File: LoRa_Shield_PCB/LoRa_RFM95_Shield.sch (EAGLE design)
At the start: 0 parts

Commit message: LoRa shield PCB power circuits
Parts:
- added B1: ARDUINO_SHIELD, SparkFun-Boards:ARDUINO_UNO_R3_SHIELDUNO_R3_SHIELD_LOCK
- added C1: 100nF, rcl:C-EUC0603
- added C10: 22uF, rcl:C-EUC0805
- added C9: 220uF, rcl:CPOL-USUD-6,3X7,7
- added D1: B5819W, dp_devices:DIODE-SOD-123
- added J1: TYPE-C-31-M-17, Type-C_Hroparts:TYPE-C-31-M-17
- added U1: RFM98W, SparkFun-RF:RFM95W
- added U2: 3V3_REG, SamacSys_Parts:AZ1117H-5.0TRE1
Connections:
- new net 3.3V: C10.2, C9.+, U1.3.3V, U2.OUT, U2.VOUT
- new net 5V: C1.1, D1.C, U2.IN
- new net GND: C1.2, C10.1, C9.-, J1.GND, J1.GND_2, J1.SHIELD, U1.GND, U2.GND
- new net N$1: D1.A, J1.VBUS, J1.VBUS_2

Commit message: update
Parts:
- removed B1: ARDUINO_SHIELD, SparkFun-Boards:ARDUINO_UNO_R3_SHIELDUNO_R3_SHIELD_LOCK
- removed C9: 220uF, rcl:CPOL-USUD-6,3X7,7
- removed J1: TYPE-C-31-M-17, Type-C_Hroparts:TYPE-C-31-M-17
- added B2: ARDUINO_SHIELD, angrypig7_Library:ARDUINO_UNO_R3_SHIELDUNO_R3_SHIELD_NOLABELS_LOCK
- added C2: 100nF, rcl:C-EUC0603
- added C3: 100uF, rcl:CPOL-USSMCB
- added J2: TYPE-C-31-M-17, angrypig7_Library:TYPE-C-31-M-17
- added JP1: (no value), pinhead_v2:PINHD-1X8/OCT
- added JP2: (no value), pinhead_v2:PINHD-1X10/OCT
- added LED1: green, adafruit:LEDCHIP-LED0603
- added R1: 10k, rcl:R-US_R0603
- added U3: 74HC4050, SparkFun-IC-Comms:HEX_CONVERTER
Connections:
- new net N$10: B2.*D11, JP2.7
- new net N$11: B2.*D10, JP2.8
- new net N$12: B2.*D9, JP2.9
- new net N$13: B2.D8, JP2.10
- new net N$14: B2.D7, JP1.1
- new net N$15: B2.*D6, JP1.2
- new net N$16: B2.*D5, JP1.3
- new net N$17: B2.D4, JP1.4
- new net N$18: B2.*D3, JP1.5
- new net N$19: B2.D2, JP1.6
- new net N$2: B2.GND@0, B2.GND@1
- new net N$20: B2.TX, JP1.7
- new net N$21: B2.RX, JP1.8
- new net N$3: B2.SCL, JP2.1
- new net N$4: LED1.A, R1.2
- new net N$5: B2.SDA, JP2.2
- new net N$6: B2.AREF, JP2.3
- new net N$7: B2.GND@2, JP2.4
- new net N$8: B2.D13, JP2.5
- new net N$9: B2.D12, JP2.6
- net 3.3V: now also C2.1, C3.+, R1.1; no longer C9.+
- net GND: now also C2.2, C3.-, J2.GND, J2.GND_2, J2.SHIELD, LED1.C; no longer C9.-, J1.GND, J1.GND_2, J1.SHIELD
- net N$1: now also J2.VBUS, J2.VBUS_2; no longer J1.VBUS, J1.VBUS_2
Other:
- moved on the sheet: C10, U1, U2

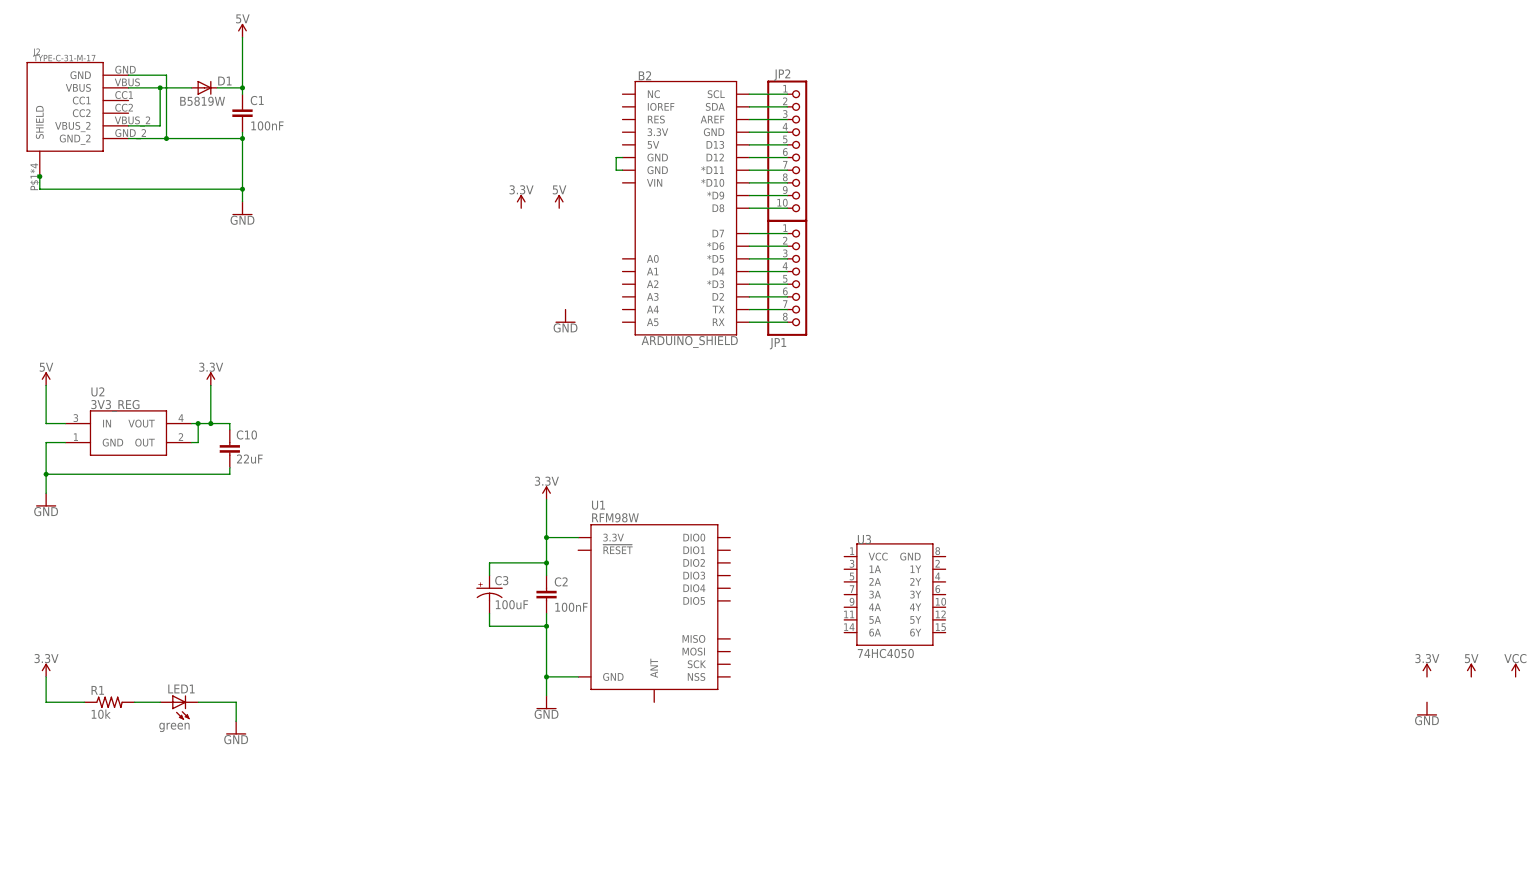
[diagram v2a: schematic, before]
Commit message: PCB artwork started
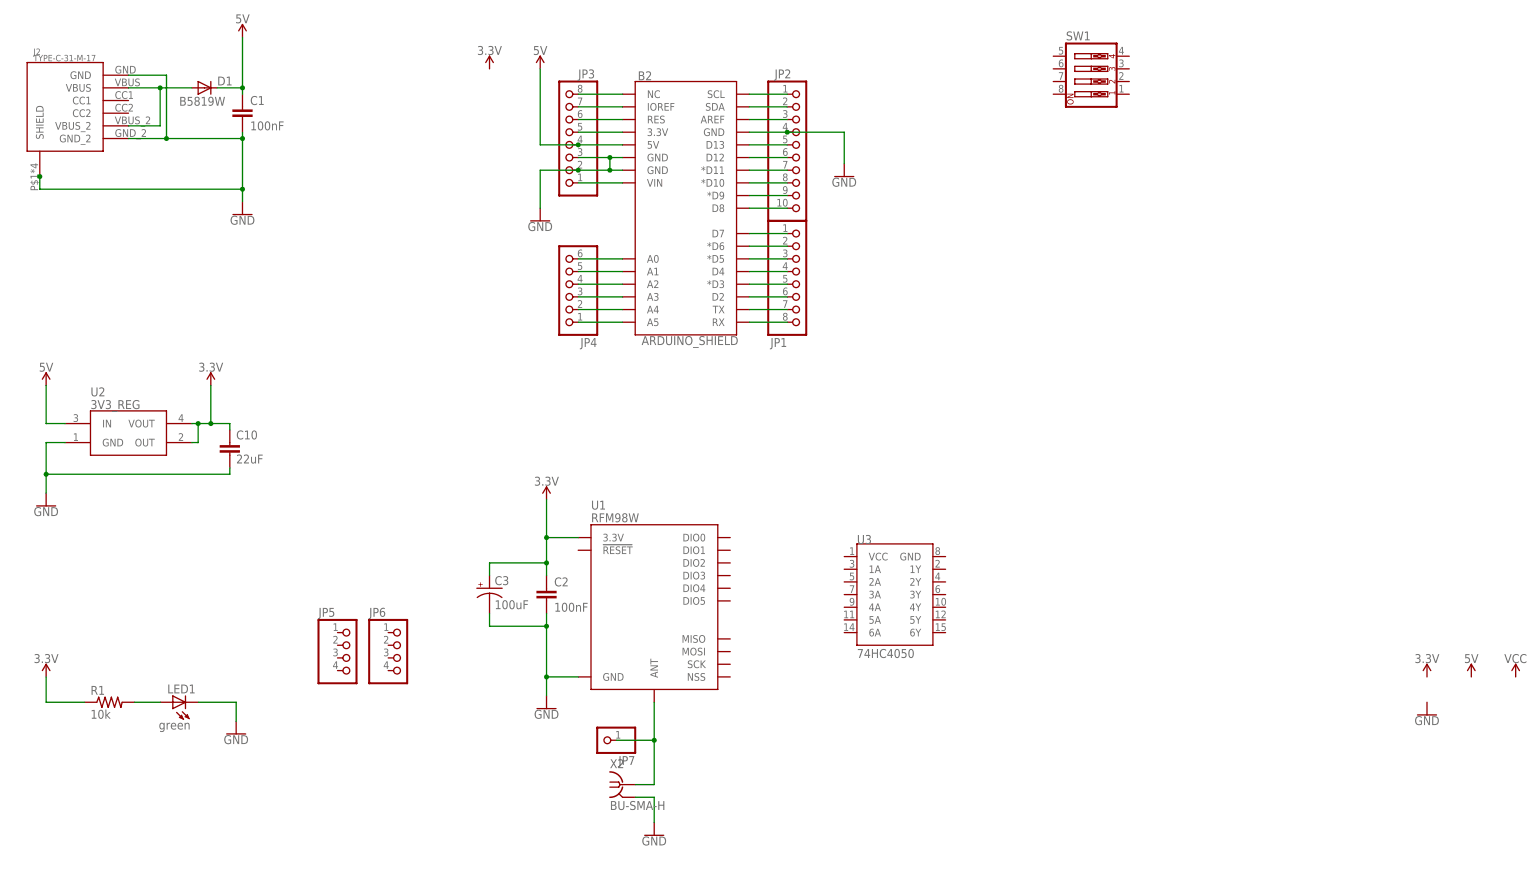
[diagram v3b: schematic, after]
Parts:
- added JP3: (no value), pinhead_v2:PINHD-1X8/OCT
- added JP4: (no value), pinhead_v2:PINHD-1X6/OCT
- added JP5, JP6: (no value), pinhead_v2:PINHD-1X4/OCT
- added JP7: (no value), pinhead_v2:PINHD-1X1/OCT
- added SW1: (no value), special:SW_DIP-4
- added X2: BU-SMA-H, con-coax:BU-SMA-H
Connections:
- new net N$23: B2.3.3V, JP3.5
- new net N$24: B2.RES, JP3.6
- new net N$25: B2.IOREF, JP3.7
- new net N$26: B2.NC, JP3.8
- new net N$27: B2.A0, JP4.6
- new net N$28: B2.A1, JP4.5
- new net N$29: B2.A2, JP4.4
- new net N$30: B2.A3, JP4.3
- new net N$31: B2.A4, JP4.2
- new net N$32: B2.A5, JP4.1
- net 5V: now also B2.5V, JP3.4
- net GND: now also B2.GND@0, B2.GND@1, B2.GND@2, JP2.4, JP3.2, JP3.3, X2.2
- net N$2: now also JP7.1, U1.ANT, X2.1; no longer B2.GND@0, B2.GND@1
- net N$7: now also B2.VIN, JP3.1; no longer B2.GND@2, JP2.4

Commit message: PCB outline
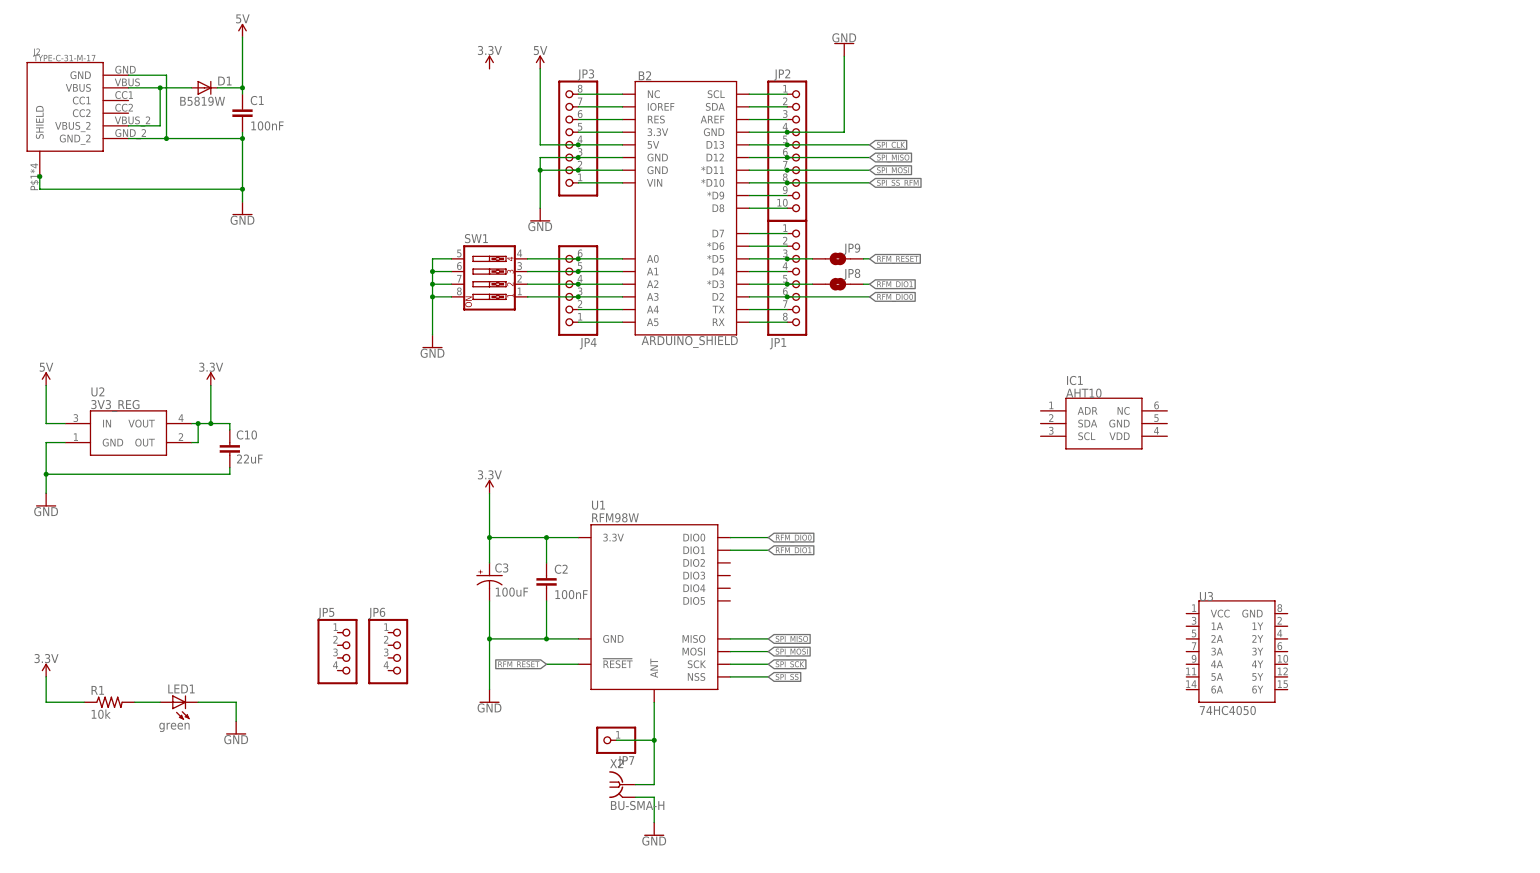
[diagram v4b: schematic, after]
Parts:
- added IC1: AHT10, SamacSys_Parts:AHT10
- added JP8, JP9: JUMPER-SMT_2_NO_SILK, SparkFun-Jumpers:JUMPER-SMT_2_NO_SILK
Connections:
- net N$11 renamed SPI_SS_RFM
- net N$8 renamed SPI_CLK
- removed net N$10 (its old number): B2.*D11, JP2.7
- removed net N$16: B2.*D5, JP1.3
- removed net N$18: B2.*D3, JP1.5
- removed net N$19: B2.D2, JP1.6
- new net N$11: B2.*D5, JP1.3, JP9.1
- new net RFM_DIO0: B2.D2, JP1.6, U1.DIO0
- new net RFM_DIO1: JP8.2, U1.DIO1
- new net RFM_RESET: JP9.2, U1.!RESET
- new net SPI_MISO: B2.D12, JP2.6, U1.MISO
- new net SPI_MOSI: B2.*D11, JP2.7, U1.MOSI
- new net SPI_SCK: U1.SCK
- new net SPI_SS: U1.NSS
- net GND: now also SW1.5, SW1.6, SW1.7, SW1.8
- net N$27: now also SW1.4
- net N$28: now also SW1.3
- net N$29: now also SW1.2
- net N$30: now also SW1.1
- net N$9: now also B2.*D3, JP1.5, JP8.1; no longer B2.D12, JP2.6
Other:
- moved on the sheet: C2, C3, SW1, U3
